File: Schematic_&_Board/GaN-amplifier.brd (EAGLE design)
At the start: 120.7 x 50.8 mm, 106 parts, among them IC1 LT3080, J1 JOHNSON_SMA_EDGE_LAUNCH_142-0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, J2 JOHNSON_SMA_EDGE_LAUNCH_142-0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, Q1 MMBT3906LT1SMD, T1 IPB080N03L G, T2 IPB080N03L G, T3 IPB080N03L G, T4 IPB080N03L G, T5 BSP89, U1 TPS7A30XX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

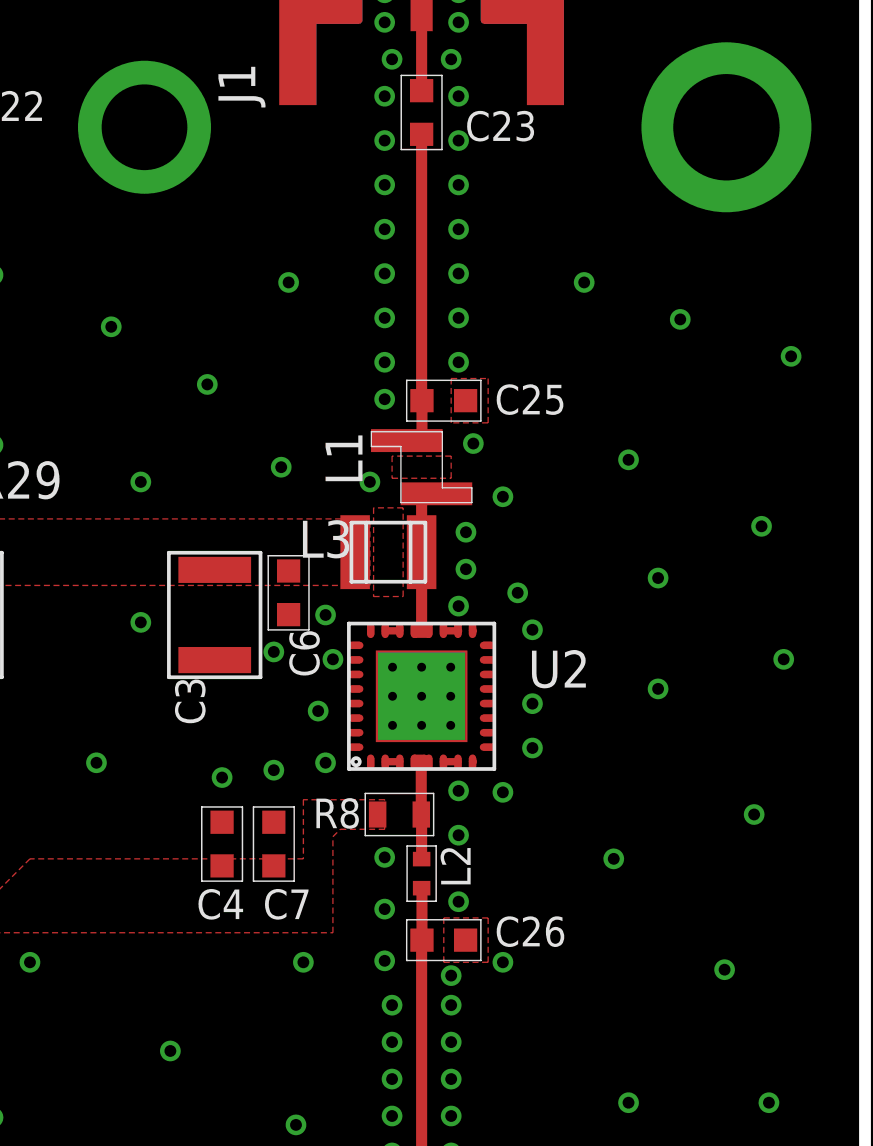
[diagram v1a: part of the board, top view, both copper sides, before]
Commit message: Moved few vias nearer to the RF microstrip
Please check that the LTC1152 is not modulating the amplitude of the RF
carrier at 4 MHz introducing sidebands.
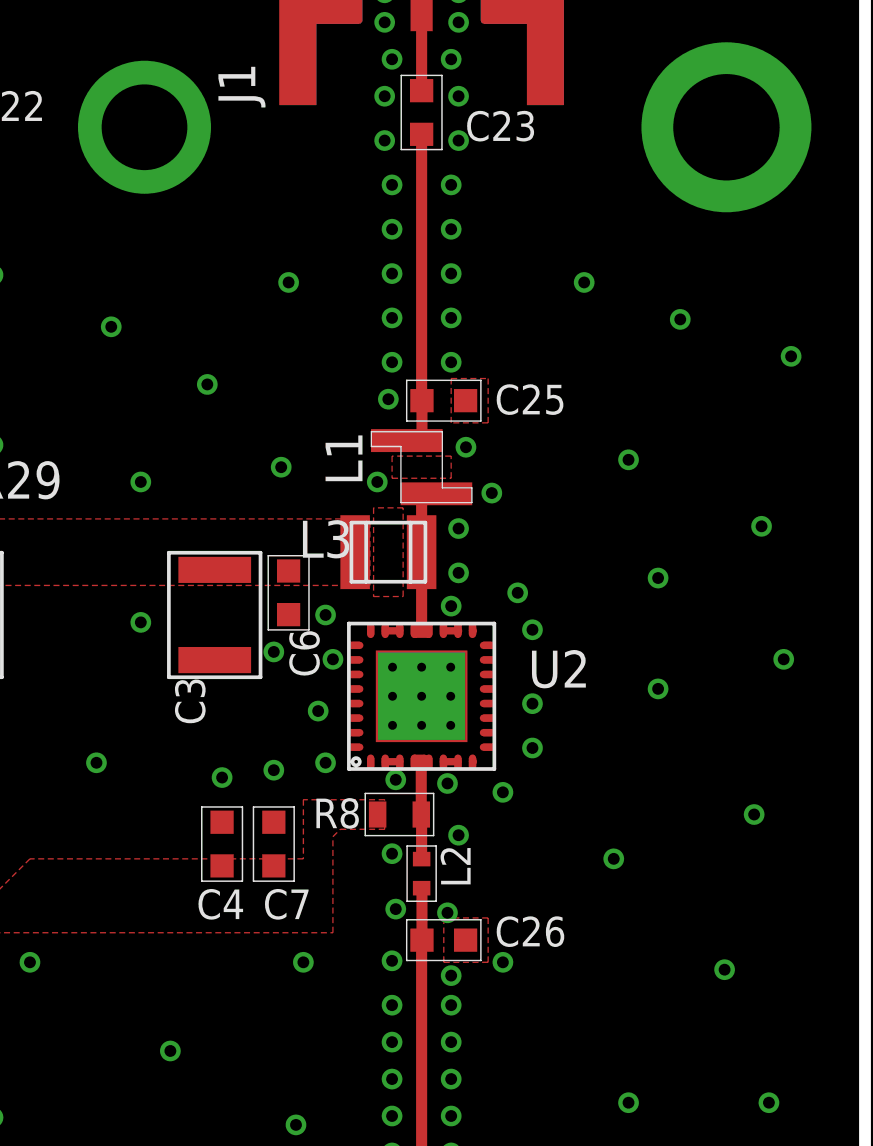
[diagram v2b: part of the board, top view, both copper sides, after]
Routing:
- net GND: vias 189 -> 190
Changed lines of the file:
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@@
 <via x="85.598" y="14.986" extent="1-16" drill="0.4064"/>
 <via x="102.108" y="28.194" extent="1-16" drill="0.4064"/>
-<via x="103.632" y="32.766" extent="1-16" drill="0.4064"/>
+<via x="103.886" y="32.766" extent="1-16" drill="0.4064"/>
 <via x="80.264" y="22.098" extent="1-16" drill="0.4064"/>
 <via x="100.33" y="26.924" extent="1-16" drill="0.4064"/>
@@
 <via x="104.394" y="13.5128" extent="1-16" drill="0.4064"/>
 <via x="104.394" y="14.7828" extent="1-16" drill="0.4064"/>
-<via x="104.14" y="16.3068" extent="1-16" drill="0.4064"/>
-<via x="104.14" y="18.0848" extent="1-16" drill="0.4064"/>
-<via x="106.68" y="22.1488" extent="1-16" drill="0.4064"/>
-<via x="104.14" y="19.8628" extent="1-16" drill="0.4064"/>
+<via x="104.394" y="16.3068" extent="1-16" drill="0.4064"/>
+<via x="104.521" y="18.0848" extent="1-16" drill="0.4064"/>
+<via x="106.299" y="22.4028" extent="1-16" drill="0.4064"/>
+<via x="104.394" y="19.9898" extent="1-16" drill="0.4064"/>
 <via x="106.68" y="20.6248" extent="1-16" drill="0.4064"/>
-<via x="106.68" y="18.3388" extent="1-16" drill="0.4064"/>
-<via x="106.934" y="29.7688" extent="1-16" drill="0.4064"/>
-<via x="106.934" y="31.0388" extent="1-16" drill="0.4064"/>
-<via x="107.188" y="34.0868" extent="1-16" drill="0.4064"/>
-<via x="104.14" y="35.6108" extent="1-16" drill="0.4064"/>
-<via x="106.68" y="36.8808" extent="1-16" drill="0.4064"/>
-<via x="104.14" y="36.8808" extent="1-16" drill="0.4064"/>
-<via x="104.14" y="38.4048" extent="1-16" drill="0.4064"/>
-<via x="106.68" y="38.4048" extent="1-16" drill="0.4064"/>
-<via x="106.68" y="39.9288" extent="1-16" drill="0.4064"/>
-<via x="104.14" y="39.9288" extent="1-16" drill="0.4064"/>
-<via x="106.68" y="41.4528" extent="1-16" drill="0.4064"/>
-<via x="104.14" y="41.4528" extent="1-16" drill="0.4064"/>
-<via x="106.68" y="42.9768" extent="1-16" drill="0.4064"/>
-<via x="104.14" y="42.9768" extent="1-16" drill="0.4064"/>
+<via x="106.299" y="17.9578" extent="1-16" drill="0.4064"/>
+<via x="106.68" y="29.6418" extent="1-16" drill="0.4064"/>
+<via x="106.68" y="31.1658" extent="1-16" drill="0.4064"/>
+<via x="106.934" y="33.9598" extent="1-16" drill="0.4064"/>
+<via x="104.267" y="35.6108" extent="1-16" drill="0.4064"/>
+<via x="106.426" y="36.8808" extent="1-16" drill="0.4064"/>
+<via x="104.394" y="36.8808" extent="1-16" drill="0.4064"/>
+<via x="104.394" y="38.4048" extent="1-16" drill="0.4064"/>
+<via x="106.426" y="38.4048" extent="1-16" drill="0.4064"/>
+<via x="106.426" y="39.9288" extent="1-16" drill="0.4064"/>
+<via x="104.394" y="39.9288" extent="1-16" drill="0.4064"/>
+<via x="106.426" y="41.4528" extent="1-16" drill="0.4064"/>
+<via x="104.394" y="41.4528" extent="1-16" drill="0.4064"/>
+<via x="106.426" y="42.9768" extent="1-16" drill="0.4064"/>
+<via x="104.394" y="42.9768" extent="1-16" drill="0.4064"/>
 <via x="106.68" y="44.5008" extent="1-16" drill="0.4064"/>
 <via x="104.14" y="44.5008" extent="1-16" drill="0.4064"/>
@@
 <via x="110.998" y="39.624" extent="1-16" drill="0.4064"/>
 <via x="108.204" y="16.256" extent="1-16" drill="0.4064"/>
-<via x="108.204" y="32.258" extent="1-16" drill="0.4064"/>
+<via x="107.823" y="32.385" extent="1-16" drill="0.4064"/>
 <via x="109.22" y="27.686" extent="1-16" drill="0.4064"/>
 <via x="113.538" y="29.464" extent="1-16" drill="0.4064"/>
@@
 </polygon>
 <via x="100.33" y="22.86" extent="1-16" drill="0.4064"/>
-<via x="106.68" y="28.4988" extent="1-16" drill="0.4064"/>
+<via x="106.426" y="28.4988" extent="1-16" drill="0.4064"/>
 <via x="98.044" y="36.1188" extent="1-16" drill="0.4064"/>
 <wire x1="104.66" y1="23.15" x2="104.16" y2="23.15" width="0.254" layer="1"/>
@@
 <contactref element="C1" pad="P$2"/>
 <contactref element="C12" pad="P$2"/>
+<via x="104.521" y="22.5298" extent="1-16" drill="0.4064"/>
 </signal>
 <signal name="N$15">

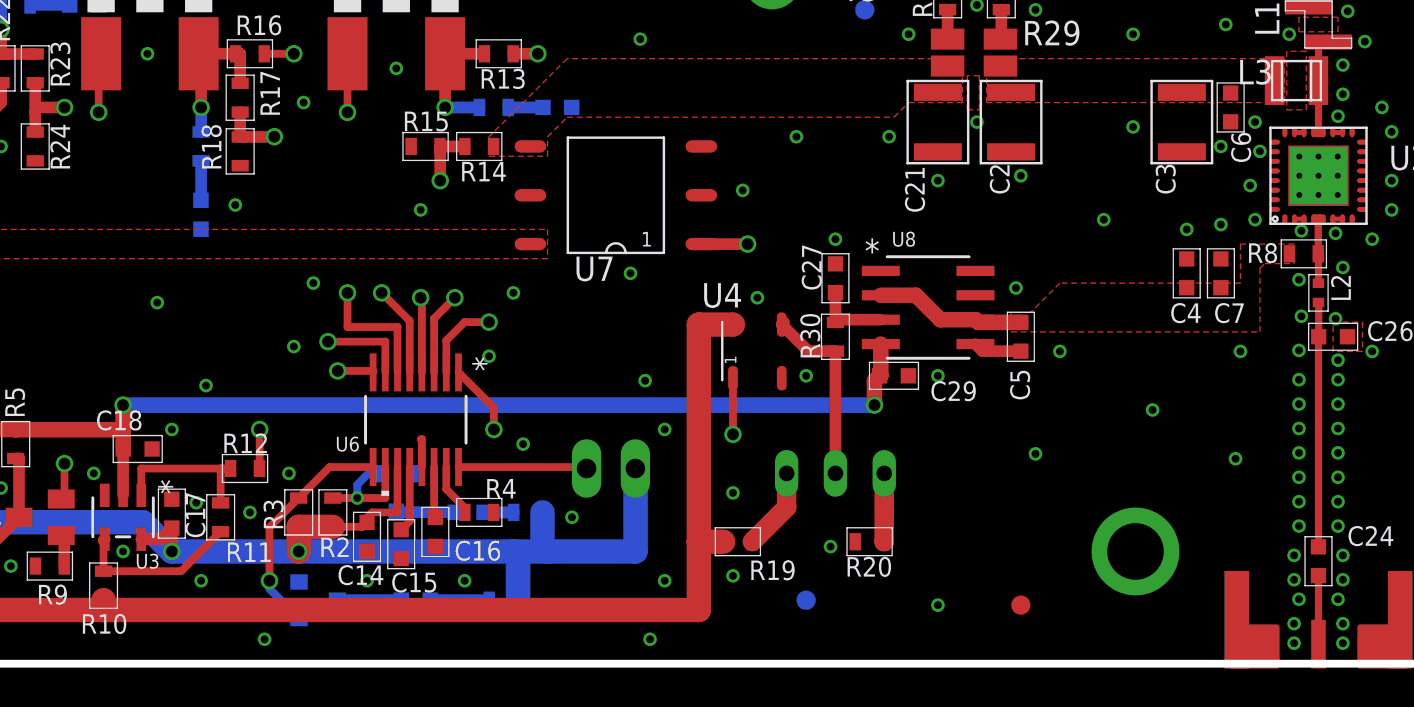
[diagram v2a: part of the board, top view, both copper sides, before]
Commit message: New Vgg Buffer
Changed out the Vgg buffer IC to reduce noise.

DSB
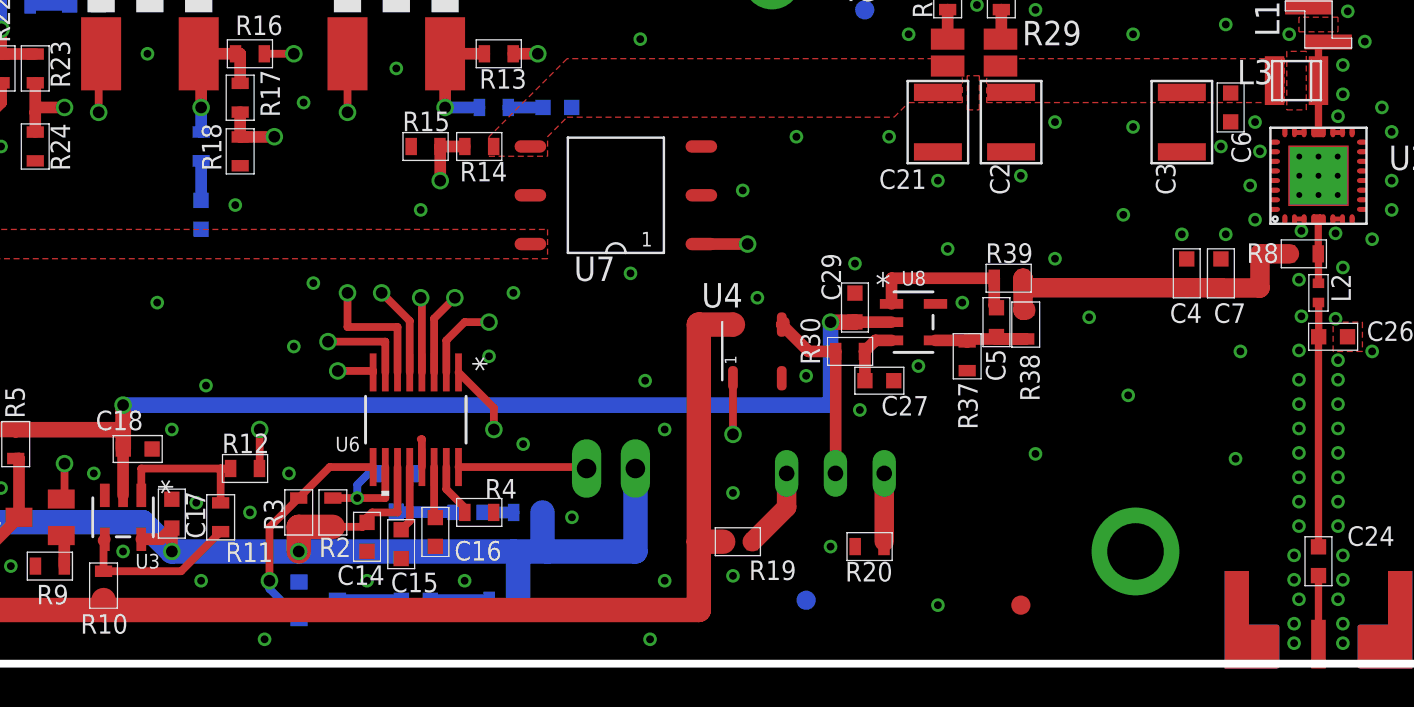
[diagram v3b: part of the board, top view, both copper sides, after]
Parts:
- added R37: 10k, jqi_passives:R_0603
- added R38: 4.02k, jqi_passives:R_0603
- added R39: 249, jqi_passives:R_0603
- C27: value 1u -> 100n
- C5: value 1n -> 150n
- R20: value 2k -> 4.02k
- R30: value 150 -> 249
- U8: value LTC1152IS8TRPBF -> LT6015; device linear-technology-jqi:SO-8_S -> linear-technology-jqi:TSOT-23_S5
- moved C27 5.80 mm to (82.5, 14.7), turned to 180 degrees
- moved C29 4.10 mm to (81.3, 18.5), turned to 270 degrees
- moved C5 1.48 mm to (88.6, 17.8)
- moved R30 1.08 mm to (81.0, 16.3), turned to 0 degrees
- moved U8 1.08 mm to (84.3, 17.8)
- moved R20 0.25 mm to (82.0, 6.10)
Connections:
- new net VMID: C5.P$2, R39.P$1, U8.1
- net AMP_POW: now also U8.2; no longer U8.4
- net GND: now also R37.P$2, U8.5; no longer U8.7
- net N$32: now also R37.P$1, R38.P$1, U8.4; no longer U8.5
- net VGG: now also R38.P$2, R39.P$2; no longer C5.P$2, U8.2, U8.6
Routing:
- net VGG: track 7.87 -> 18.0 mm
- net VMID: track 0.00 -> 8.27 mm
- net N$32: track 2.52 -> 6.44 mm
- net AMP_POW: track 62.1 -> 64.0 mm
- net N$43: track 4.05 -> 3.18 mm
- net GND: vias 190 -> 193
- removed copper zone on layer 1, net VGG

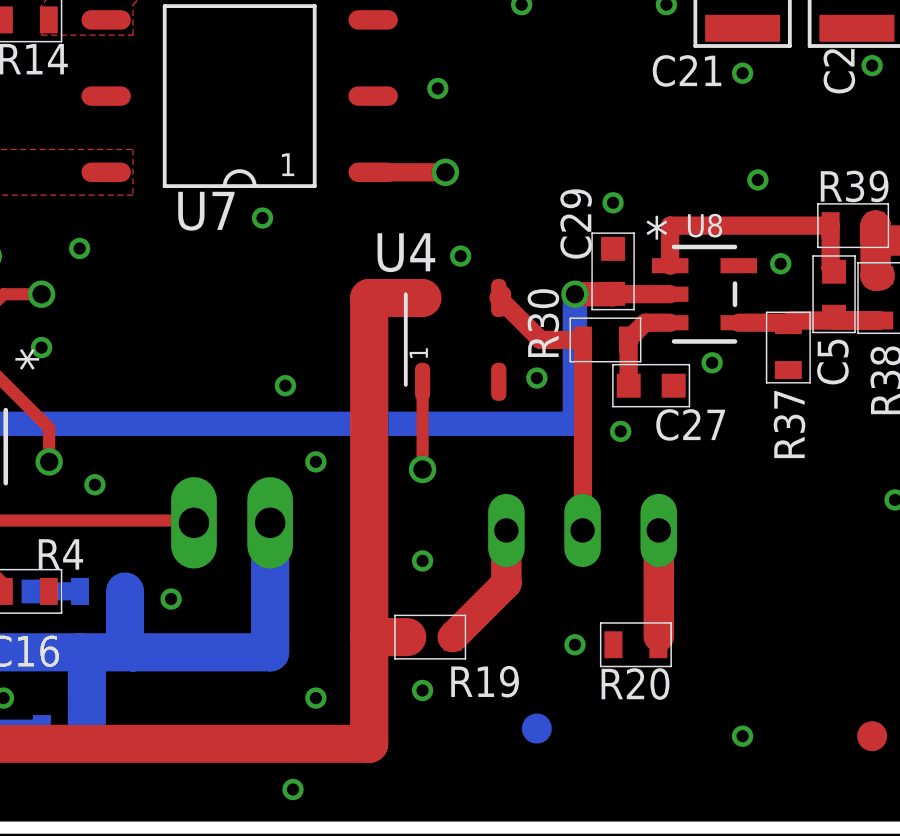
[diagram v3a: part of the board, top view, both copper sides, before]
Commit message: Fixed U4 package
Updated board layout with correct optomos package.

DSB
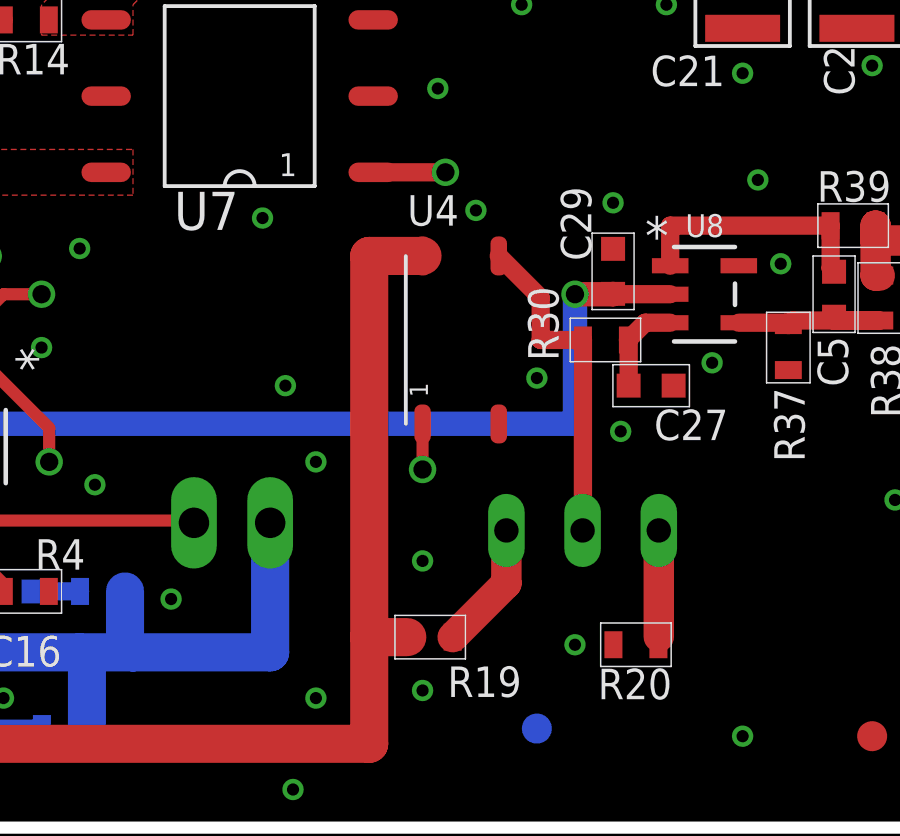
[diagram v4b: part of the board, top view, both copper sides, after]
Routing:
- net -8V: track 80.4 -> 81.8 mm
- net N$16: track 35.5 -> 34.1 mm
- net V_PINCH: track 9.90 -> 11.1 mm
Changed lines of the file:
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@@
 <element name="U4" library="transistor-jqi" package="4-LEAD_SOP" value="CPC1117NTR" x="76.2" y="16.256" smashed="yes" rot="R90">
 <attribute name="PARTNO" value="CPC1117NTR" x="76.2" y="16.256" size="1.778" layer="27" rot="R90" display="off"/>
-<attribute name="NAME" x="75.438" y="19.812" size="1.27" layer="25" rot="R180"/>
+<attribute name="NAME" x="74.422" y="20.066" size="1.016" layer="25"/>
 </element>
 <element name="Q1" library="transistor-pnp" package="SOT23-BEC" value="MMBT3906LT1SMD" x="38.862" y="7.62" smashed="yes" rot="R90">
@@
 <via x="78.232" y="27.432" extent="1-16" drill="0.4064"/>
 <via x="83.058" y="27.432" extent="1-16" drill="0.4064"/>
-<via x="76.2" y="19.05" extent="1-16" drill="0.4064"/>
+<via x="76.708" y="20.574" extent="1-16" drill="0.4064"/>
 <via x="58.674" y="23.622" extent="1-16" drill="0.4064"/>
 <via x="106.68" y="2.0828" extent="1-16" drill="0.4064"/>
@@
 <wire x1="42.164" y1="3.314" x2="42.164" y2="2.794" width="1.27" layer="1"/>
 <wire x1="42.164" y1="2.794" x2="73.152" y2="2.794" width="1.27" layer="1"/>
-<wire x1="74.93" y1="17.653" x2="73.152" y2="17.653" width="1.27" layer="1"/>
-<wire x1="73.152" y1="17.653" x2="73.152" y2="6.35" width="1.27" layer="1"/>
+<wire x1="73.152" y1="19.05635" x2="73.152" y2="6.35" width="1.27" layer="1"/>
 <wire x1="73.152" y1="6.35" x2="73.152" y2="2.794" width="1.27" layer="1"/>
 <wire x1="74.434" y1="6.35" x2="74.422" y2="6.35" width="0.6096" layer="1"/>
@@
 <wire x1="17.272" y1="5.334" x2="23.241" y2="5.334" width="0.6096" layer="1"/>
 <wire x1="23.241" y1="5.334" x2="23.241" y2="7.239" width="0.6096" layer="1"/>
+<wire x1="73.152" y1="19.05635" x2="74.93" y2="19.05635" width="1.27" layer="1"/>
 </signal>
 <signal name="VPIN_DET">
@@
 <wire x1="55.118" y1="31.75" x2="74.93" y2="11.938" width="0.4064" layer="2"/>
 <via x="74.93" y="11.938" extent="1-16" drill="0.6096"/>
-<wire x1="74.93" y1="11.938" x2="74.93" y2="14.859" width="0.4064" layer="1"/>
+<wire x1="74.93" y1="11.938" x2="74.93" y2="13.45565" width="0.4064" layer="1"/>
 </signal>
 <signal name="N$19">
@@
 <signal name="V_PINCH">
 <contactref element="U4" pad="P$3"/>
-<wire x1="77.47" y1="17.653" x2="77.585" y2="17.768" width="0.6096" layer="1"/>
 <contactref element="R21" pad="2"/>
 <contactref element="R30" pad="P$1"/>
 <wire x1="80.276" y1="16.256" x2="78.867" y2="16.256" width="0.6096" layer="1"/>
-<wire x1="78.867" y1="16.256" x2="77.47" y2="17.653" width="0.6096" layer="1"/>
 <wire x1="80.276" y1="16.256" x2="80.276" y2="9.918" width="0.6096" layer="1"/>
 <wire x1="80.276" y1="9.918" x2="80.264" y2="9.906" width="0.6096" layer="1"/>
+<wire x1="78.867" y1="16.256" x2="78.867" y2="17.65935" width="0.6096" layer="1"/>
+<wire x1="78.867" y1="17.65935" x2="77.47" y2="19.05635" width="0.6096" layer="1"/>
 </signal>
 <signal name="VGG">
